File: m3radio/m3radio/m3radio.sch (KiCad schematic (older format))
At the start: 13 parts

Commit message: Finished schematics
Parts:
- removed C?: 4.7uF, symbol C
- removed C? (x5): 100nF, symbol C
- removed C?: 1uF, symbol C
- removed C? (x2): 2.2uF, symbol C
- removed STM32F405RGTB: STM32F405RXTX, agg:LQFP-64, symbol STM32F405RXTX
- added C? (x6): 100n, agg:0402, symbol C
- added C? (x2): 2µ2, agg:0402, symbol C
- added C? (x2): 10p, agg:0402, symbol C
- added C?: 1µ, agg:0402, symbol C
- added C?: 4µ7, agg:0402, symbol C
- added D?: RED, agg:0603-LED, symbol LED
- added D?: GRN, agg:0603-LED, symbol LED
- added IC?: MCP2562, agg:DFN-8-EP-MICROCHIP, symbol MCP2562
- added IC?: STM32F405RxTx, agg:LQFP-64, symbol STM32F405RxTx
- added J?: EAST TOP, agg:TFML-110-02-L-D, symbol CONN_02x10
- added J?: EAST BOT, agg:SFML-110-02-L-D-LC, symbol CONN_02x10
- added J?: WEST TOP, agg:TFML-110-02-L-D, symbol CONN_02x10
- added J?: WEST BOT, agg:SFML-110-02-L-D-LC, symbol CONN_02x10
- added R? (x3): 100, agg:0402, symbol R
- added Y?: 26M, agg:XTAL-20x16, symbol SMD_XTAL
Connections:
- net labels added: 3v3_AUX1, 3v3_AUX2, 3v3_DL, 3v3_FC, 3v3_IMU, 3v3_PYRO, 3v3_RADIO, 5v_AUX1, 5v_AUX2, 5v_CAM, 5v_CAN, 5v_IMU, 5v_RADIO, CAN+, CAN-, CAN_RXD, CAN_TXD, CHARGE, JTCK, JTDI, JTDO, JTDR, JTMS, LED_GRN, LED_RED, PWR, PYRO1, PYRO2, PYRO3, PYRO4, PYRO_SI, PYRO_SO, RSVD1, RSVD2, ~RST
- net labels removed: VDD
- wire segments 60 -> 199
- no-connect marks 7 -> 41
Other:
- note added: "INTERCONNECTS"
- note added: "PB4 is JTRST, \nDO NOT CONNECT (Errata 2.1.4)"
- note removed: "STM32F405 rgt6"

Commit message: Started PCB layout
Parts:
- gave numbers to parts that had none: 27

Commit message: Moved MAX-q7 to usable component library
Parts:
- IC103: footprint agg-unchecked:MAX-7Q -> M3radio:MAX-7Q
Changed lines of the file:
@@
 F 0 "IC103" H 8950 2400 50  0000 L CNN
 F 1 "MAX-7Q" H 8950 1200 50  0000 L CNN
-F 2 "agg-unchecked:MAX-7Q" H 8950 1100 50  0001 L CNN
+F 2 "M3radio:MAX-7Q" H 8950 1100 50  0001 L CNN
 F 3 "" H 9300 1900 50  0001 C CNN
 F 4 "MAX-7Q" H 8950 1000 50  0001 L CNN "HabSupplies"

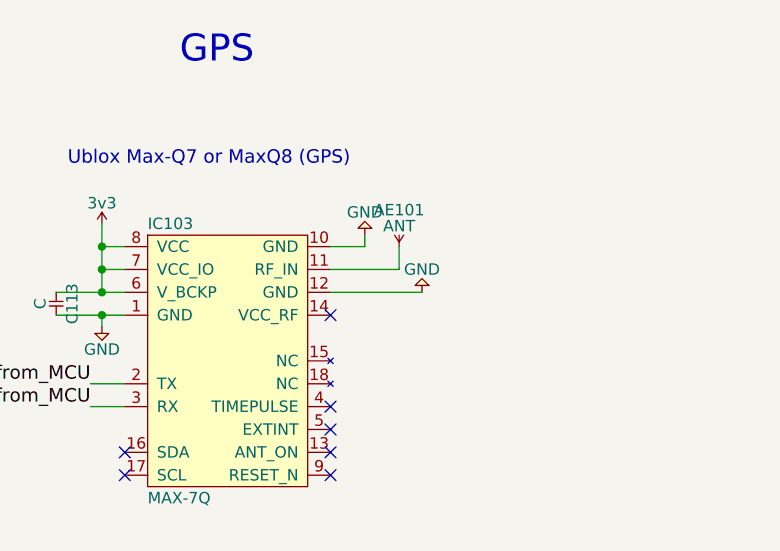
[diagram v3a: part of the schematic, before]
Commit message: Added footprints missing for various passives
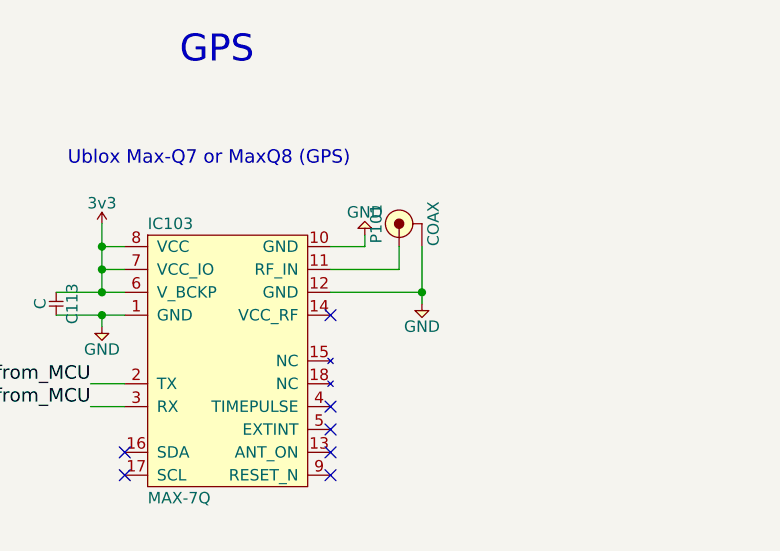
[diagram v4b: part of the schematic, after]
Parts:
- removed AE101: ANT, symbol ANT
- added P101: COAX, M3radio:SMA-142-0701-801, symbol COAX
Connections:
- net GND: now also P101.2 (GND)
- net at IC103.11 (RF_IN): now also P101.1 (RF)
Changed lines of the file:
@@
-$EndComp
-$Comp
-L ANT AE101
-U 1 1 56B21382
-P 10050 1500
-F 0 "AE101" H 10050 1660 50  0000 C CNN
-F 1 "ANT" H 10050 1590 50  0000 C CNN
-F 2 "" H 10050 1500 50  0001 C CNN
-F 3 "" H 10050 1500 50  0001 C CNN
-	1    10050 1500
-	1    0    0    -1
 $EndComp
 $Comp
@@
 F 3 "" H 9900 1450 118 0000 C CNN
 	1    9900 1450
-	-1   0    0    1
-$EndComp
-$Comp
-L GND #PWR04
-U 1 1 56B213F7
-P 10150 1700
-F 0 "#PWR04" H 10020 1740 50  0001 L CNN
-F 1 "GND" H 10150 1600 50  0000 C CNN
-F 2 "" H 10150 1700 118 0000 C CNN
-F 3 "" H 10150 1700 118 0000 C CNN
-	1    10150 1700
 	-1   0    0    1
 $EndComp
@@
 $EndComp
 $Comp
-L GND #PWR05
+L GND #PWR04
 U 1 1 56C563A9
 P 5400 2050
-F 0 "#PWR05" H 5270 2090 50  0001 L CNN
+F 0 "#PWR04" H 5270 2090 50  0001 L CNN
 F 1 "GND" H 5400 1950 50  0000 C CNN
 F 2 "" H 5400 2050 60  0000 C CNN
@@
 $EndComp
 $Comp
-L GND #PWR06
+L GND #PWR05
 U 1 1 56C563AF
 P 5000 2050
-F 0 "#PWR06" H 4870 2090 50  0001 L CNN
+F 0 "#PWR05" H 4870 2090 50  0001 L CNN
 F 1 "GND" H 5000 1950 50  0000 C CNN
 F 2 "" H 5000 2050 60  0000 C CNN
@@
 $EndComp
 $Comp
-L GND #PWR07
+L GND #PWR06
 U 1 1 56C563B5
 P 5000 1050
-F 0 "#PWR07" H 4870 1090 50  0001 L CNN
+F 0 "#PWR06" H 4870 1090 50  0001 L CNN
 F 1 "GND" H 5000 950 50  0000 C CNN
 F 2 "" H 5000 1050 60  0000 C CNN
@@
 $EndComp
 $Comp
-L GND #PWR08
+L GND #PWR07
 U 1 1 56C563BB
 P 5400 1050
-F 0 "#PWR08" H 5270 1090 50  0001 L CNN
+F 0 "#PWR07" H 5270 1090 50  0001 L CNN
 F 1 "GND" H 5400 950 50  0000 C CNN
 F 2 "" H 5400 1050 60  0000 C CNN
@@
 $EndComp
 $Comp
-L GND #PWR09
+L GND #PWR08
 U 1 1 56C563C1
 P 6400 2050
-F 0 "#PWR09" H 6270 2090 50  0001 L CNN
+F 0 "#PWR08" H 6270 2090 50  0001 L CNN
 F 1 "GND" H 6400 1950 50  0000 C CNN
 F 2 "" H 6400 2050 60  0000 C CNN
@@
 $EndComp
 $Comp
-L GND #PWR010
+L GND #PWR09
 U 1 1 56C563C7
 P 6800 2050
-F 0 "#PWR010" H 6670 2090 50  0001 L CNN
+F 0 "#PWR09" H 6670 2090 50  0001 L CNN
 F 1 "GND" H 6800 1950 50  0000 C CNN
 F 2 "" H 6800 2050 60  0000 C CNN
@@
 $EndComp
 $Comp
-L GND #PWR011
+L GND #PWR010
 U 1 1 56C563CD
 P 6400 1050
-F 0 "#PWR011" H 6270 1090 50  0001 L CNN
+F 0 "#PWR010" H 6270 1090 50  0001 L CNN
 F 1 "GND" H 6400 950 50  0000 C CNN
 F 2 "" H 6400 1050 60  0000 C CNN
@@
 $EndComp
 $Comp
-L GND #PWR012
+L GND #PWR011
 U 1 1 56C563D3
 P 6800 1050
-F 0 "#PWR012" H 6670 1090 50  0001 L CNN
+F 0 "#PWR011" H 6670 1090 50  0001 L CNN
 F 1 "GND" H 6800 950 50  0000 C CNN
 F 2 "" H 6800 1050 60  0000 C CNN
@@
 CAN+
 $Comp
-L GND #PWR013
+L GND #PWR012
 U 1 1 56C563E5
 P 5400 3350
-F 0 "#PWR013" H 5270 3390 50  0001 L CNN
+F 0 "#PWR012" H 5270 3390 50  0001 L CNN
 F 1 "GND" H 5400 3250 50  0000 C CNN
 F 2 "" H 5400 3350 60  0000 C CNN
@@
 $EndComp
 $Comp
-L GND #PWR014
+L GND #PWR013
 U 1 1 56C563EB
 P 5000 3350
-F 0 "#PWR014" H 4870 3390 50  0001 L CNN
+F 0 "#PWR013" H 4870 3390 50  0001 L CNN
 F 1 "GND" H 5000 3250 50  0000 C CNN
 F 2 "" H 5000 3350 60  0000 C CNN
@@
 $EndComp
 $Comp
-L GND #PWR015
+L GND #PWR014
 U 1 1 56C563F1
 P 5000 2350
-F 0 "#PWR015" H 4870 2390 50  0001 L CNN
+F 0 "#PWR014" H 4870 2390 50  0001 L CNN
 F 1 "GND" H 5000 2250 50  0000 C CNN
 F 2 "" H 5000 2350 60  0000 C CNN
@@
 $EndComp
 $Comp
-L GND #PWR016
+L GND #PWR015
 U 1 1 56C563F7
 P 5400 2350
-F 0 "#PWR016" H 5270 2390 50  0001 L CNN
+F 0 "#PWR015" H 5270 2390 50  0001 L CNN
 F 1 "GND" H 5400 2250 50  0000 C CNN
 F 2 "" H 5400 2350 60  0000 C CNN
@@
 $EndComp
 $Comp
-L GND #PWR017
+L GND #PWR016
 U 1 1 56C56421
 P 6400 3350
-F 0 "#PWR017" H 6270 3390 50  0001 L CNN
+F 0 "#PWR016" H 6270 3390 50  0001 L CNN
 F 1 "GND" H 6400 3250 50  0000 C CNN
 F 2 "" H 6400 3350 60  0000 C CNN
@@
 $EndComp
 $Comp
-L GND #PWR018
+L GND #PWR017
 U 1 1 56C56427
 P 6800 3350
-F 0 "#PWR018" H 6670 3390 50  0001 L CNN
+F 0 "#PWR017" H 6670 3390 50  0001 L CNN
 F 1 "GND" H 6800 3250 50  0000 C CNN
 F 2 "" H 6800 3350 60  0000 C CNN
@@
 $EndComp
 $Comp
-L GND #PWR019
+L GND #PWR018
 U 1 1 56C5642D
 P 6400 2350
-F 0 "#PWR019" H 6270 2390 50  0001 L CNN
+F 0 "#PWR018" H 6270 2390 50  0001 L CNN
 F 1 "GND" H 6400 2250 50  0000 C CNN
 F 2 "" H 6400 2350 60  0000 C CNN
@@
 $EndComp
 $Comp
-L GND #PWR020
+L GND #PWR019
 U 1 1 56C56433
 P 6800 2350
-F 0 "#PWR020" H 6670 2390 50  0001 L CNN
+F 0 "#PWR019" H 6670 2390 50  0001 L CNN
 F 1 "GND" H 6800 2250 50  0000 C CNN
 F 2 "" H 6800 2350 60  0000 C CNN
@@
 INTERCONNECTS
 $Comp
-L 3v3 #PWR021
+L 3v3 #PWR020
 U 1 1 56C5644A
 P 5800 2050
-F 0 "#PWR021" H 5800 2160 50  0001 L CNN
+F 0 "#PWR020" H 5800 2160 50  0001 L CNN
 F 1 "3v3" H 5800 2140 50  0000 C CNN
 F 2 "" H 5800 2050 60  0000 C CNN
@@
 $EndComp
 $Comp
-L GND #PWR022
+L GND #PWR021
 U 1 1 56C56451
 P 5800 2350
-F 0 "#PWR022" H 5670 2390 50  0001 L CNN
+F 0 "#PWR021" H 5670 2390 50  0001 L CNN
 F 1 "GND" H 5800 2250 50  0000 C CNN
 F 2 "" H 5800 2350 60  0000 C CNN
@@
 $EndComp
 $Comp
-L 3v3 #PWR023
+L 3v3 #PWR022
 U 1 1 56C56457
 P 2050 6350
-F 0 "#PWR023" H 2050 6460 50  0001 L CNN
+F 0 "#PWR022" H 2050 6460 50  0001 L CNN
 F 1 "3v3" H 2050 6440 50  0000 C CNN
 F 2 "" H 2050 6350 60  0000 C CNN
@@
 5v_CAN
 $Comp
-L GND #PWR024
+L GND #PWR023
 U 1 1 56C5645E
 P 2050 6850
-F 0 "#PWR024" H 1920 6890 50  0001 L CNN
+F 0 "#PWR023" H 1920 6890 50  0001 L CNN
 F 1 "GND" H 2050 6750 50  0000 C CNN
 F 2 "" H 2050 6850 60  0000 C CNN
@@
 $EndComp
 $Comp
-L GND #PWR025
+L GND #PWR024
 U 1 1 56C564FE
 P 6200 4600
-F 0 "#PWR025" H 6070 4640 50  0001 L CNN
+F 0 "#PWR024" H 6070 4640 50  0001 L CNN
 F 1 "GND" H 6200 4500 50  0000 C CNN
 F 2 "" H 6200 4600 60  0000 C CNN
@@
 $EndComp
 $Comp
-L GND #PWR026
+L GND #PWR025
 U 1 1 56C5650A
 P 6200 4950
-F 0 "#PWR026" H 6070 4990 50  0001 L CNN
+F 0 "#PWR025" H 6070 4990 50  0001 L CNN
 F 1 "GND" H 6200 4850 50  0000 C CNN
 F 2 "" H 6200 4950 60  0000 C CNN
@@
 ~RST
 $Comp
-L GND #PWR027
+L GND #PWR026
 U 1 1 56C5654A
 P 1550 2600
-F 0 "#PWR027" H 1420 2640 50  0001 L CNN
+F 0 "#PWR026" H 1420 2640 50  0001 L CNN
 F 1 "GND" H 1550 2500 50  0000 C CNN
 F 2 "" H 1550 2600 60  0000 C CNN
@@
 $EndComp
 $Comp
-L GND #PWR028
+L GND #PWR027
 U 1 1 56C56560
 P 1200 2200
-F 0 "#PWR028" H 1070 2240 50  0001 L CNN
+F 0 "#PWR027" H 1070 2240 50  0001 L CNN
 F 1 "GND" H 1200 2100 50  0000 C CNN
 F 2 "" H 1200 2200 60  0000 C CNN
@@
 $EndComp
 $Comp
-L GND #PWR029
+L GND #PWR028
 U 1 1 56C56566
 P 1200 2300
-F 0 "#PWR029" H 1070 2340 50  0001 L CNN
+F 0 "#PWR028" H 1070 2340 50  0001 L CNN
 F 1 "GND" H 1200 2200 50  0000 C CNN
 F 2 "" H 1200 2300 60  0000 C CNN
@@
 $EndComp
 $Comp
-L GND #PWR030
+L GND #PWR029
 U 1 1 56C56584
 P 800 2800
-F 0 "#PWR030" H 670 2840 50  0001 L CNN
+F 0 "#PWR029" H 670 2840 50  0001 L CNN
 F 1 "GND" H 800 2700 50  0000 C CNN
 F 2 "" H 800 2800 60  0000 C CNN
@@
 Connection ~ 1450 1200
 $Comp
-L GND #PWR031
+L GND #PWR030
 U 1 1 56C5669F
 P 1050 1750
-F 0 "#PWR031" H 920 1790 50  0001 L CNN
+F 0 "#PWR030" H 920 1790 50  0001 L CNN
 F 1 "GND" H 1050 1650 50  0000 C CNN
 F 2 "" H 1050 1750 60  0000 C CNN
@@
 Connection ~ 1050 1200
 $Comp
-L 3v3 #PWR032
+L 3v3 #PWR031
 U 1 1 56C566B3
 P 1550 1050
-F 0 "#PWR032" H 1550 1160 50  0001 L CNN
+F 0 "#PWR031" H 1550 1160 50  0001 L CNN
 F 1 "3v3" H 1550 1140 50  0000 C CNN
 F 2 "" H 1550 1050 60  0000 C CNN
@@
 Connection ~ 1550 1600
 $Comp
-L GND #PWR033
+L GND #PWR032
 U 1 1 56C566C1
 P 1450 2000
-F 0 "#PWR033" H 1320 2040 50  0001 L CNN
+F 0 "#PWR032" H 1320 2040 50  0001 L CNN
 F 1 "GND" H 1450 1900 50  0000 C CNN
 F 2 "" H 1450 2000 60  0000 C CNN
@@
 NoConn ~ 2600 1200
 $Comp
-L PWR #FLG034
+L PWR #FLG033
 U 1 1 56C5671C
 P 5750 2100
-F 0 "#FLG034" H 5750 2260 50  0001 C CNN
+F 0 "#FLG033" H 5750 2260 50  0001 C CNN
 F 1 "PWR" H 5750 2190 50  0000 C CNN
 F 2 "" H 5750 2100 50  0001 C CNN
@@
 $EndComp
 $Comp
-L PWR #FLG035
+L PWR #FLG034
 U 1 1 56C56722
 P 5800 2300
-F 0 "#FLG035" H 5800 2460 50  0001 C CNN
+F 0 "#FLG034" H 5800 2460 50  0001 C CNN
 F 1 "PWR" H 5800 2390 50  0000 C CNN
 F 2 "" H 5800 2300 50  0001 C CNN
@@
 $EndComp
 $Comp
-L PWR #FLG036
+L PWR #FLG035
 U 1 1 56C56728
 P 1550 6500
-F 0 "#FLG036" H 1550 6660 50  0001 C CNN
+F 0 "#FLG035" H 1550 6660 50  0001 C CNN
 F 1 "PWR" H 1550 6590 50  0000 C CNN
 F 2 "" H 1550 6500 50  0001 C CNN
@@
 3v3_RADIO
 NoConn ~ 1600 3800
+$Comp
+L COAX P101
+U 1 1 56C710D6
+P 10050 1400
+F 0 "P101" H 10050 1500 50  0000 C CNN
+F 1 "COAX" H 10050 1250 50  0000 C CNN
+F 2 "M3radio:SMA-142-0701-801" H 10050 1190 50  0001 C CNN
+F 3 "" H 10150 1300 50  0001 C CNN
+F 4 "1608592" H 10050 1120 50  0001 C CNN "Farnell"
+	1    10050 1400
+	0    -1   -1   0
+$EndComp
+Wire Wire Line
+	10150 1500 10150 1750
+Connection ~ 10150 1700
+$Comp
+L GND #PWR036
+U 1 1 56C71AF7
+P 10150 1750
+F 0 "#PWR036" H 10020 1790 50  0001 L CNN
+F 1 "GND" H 10150 1650 50  0000 C CNN
+F 2 "" H 10150 1750 60  0000 C CNN
+F 3 "" H 10150 1750 60  0000 C CNN
+	1    10150 1750
+	1    0    0    -1
+$EndComp
 $EndSCHEMATC

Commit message: Changed inductor size and found Farnell codes
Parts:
- C113: footprint (none) -> agg:0402
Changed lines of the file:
@@
 F 0 "C113" H 8600 1770 50  0000 C CNN
 F 1 "C" H 8600 1630 50  0000 C CNN
-F 2 "" H 8550 1700 50  0001 C CNN
+F 2 "agg:0402" H 8550 1700 50  0001 C CNN
 F 3 "" H 8550 1700 50  0001 C CNN
 	1    8550 1700

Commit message: Major changes to layout.
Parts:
- P101: footprint M3radio:SMA-142-0701-801 -> (none); Fieldname (none) -> Value
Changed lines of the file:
@@
 PB4 is JTRST, \nDO NOT CONNECT (Errata 2.1.4)
 NoConn ~ 2600 1500
-Text Label 1500 2500 2    60   ~ 0
-~RST
 $Comp
 L GND #PWR026
@@
 F 0 "P101" H 10050 1500 50  0000 C CNN
 F 1 "COAX" H 10050 1250 50  0000 C CNN
-F 2 "M3radio:SMA-142-0701-801" H 10050 1190 50  0001 C CNN
+F 2 "" H 10050 1190 50  0001 C CNN
 F 3 "" H 10150 1300 50  0001 C CNN
-F 4 "1608592" H 10050 1120 50  0001 C CNN "Farnell"
+F 4 "Value" H 10050 1400 60  0001 C CNN "Fieldname"
+F 5 "1608592" H 10050 1120 50  0001 C CNN "Farnell"
 	1    10050 1400
 	0    -1   -1   0
@@
 	1    0    0    -1
 $EndComp
+Text Label 1500 2500 2    60   ~ 0
+~RST
 $EndSCHEMATC
